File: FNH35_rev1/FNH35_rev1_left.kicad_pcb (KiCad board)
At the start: 2 copper layers, 127.2 x 116.7 mm, 117 parts, among them IC1 NUF2221W1T2G, J101 Conn_01x03, J102 DX07B024JJ3R1600, J103 Conn_01x08, K201 KEYSW, K202 KEYSW, K203 KEYSW, K204 KEYSW, K205 KEYSW, K206 KEYSW, K207 KEYSW, K208 KEYSW, K209 KEYSW, K210 KEYSW, K211 KEYSW, K212 KEYSW, K213 KEYSW, K214 KEYSW, K215 KEYSW, K216 KEYSW, K217 KEYSW, K218 KEYSW, SW101 SW_PUSH, U101 LD1117S33TR_SOT223, U102 STM32F303CCTx, U103 74AHCT125, X101 XTAL_GND

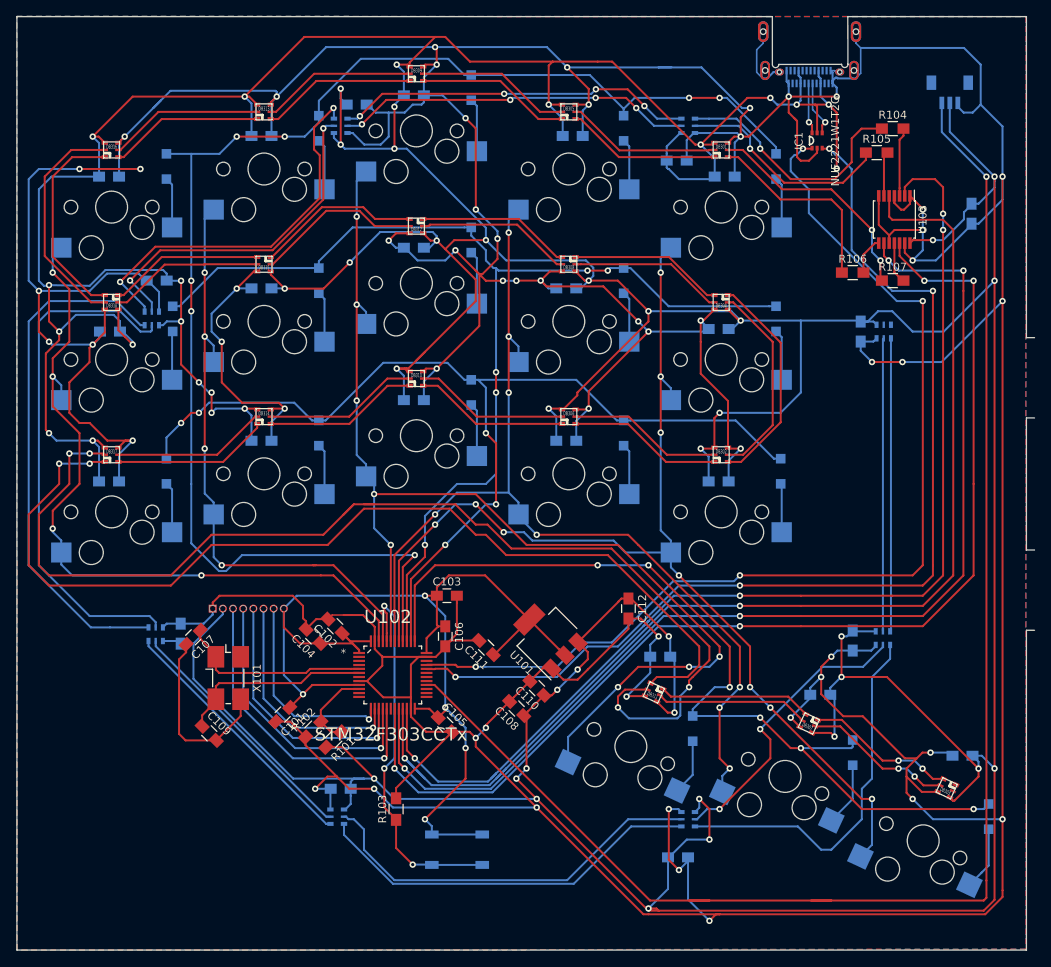
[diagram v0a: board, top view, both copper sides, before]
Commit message: left half crystal reworked
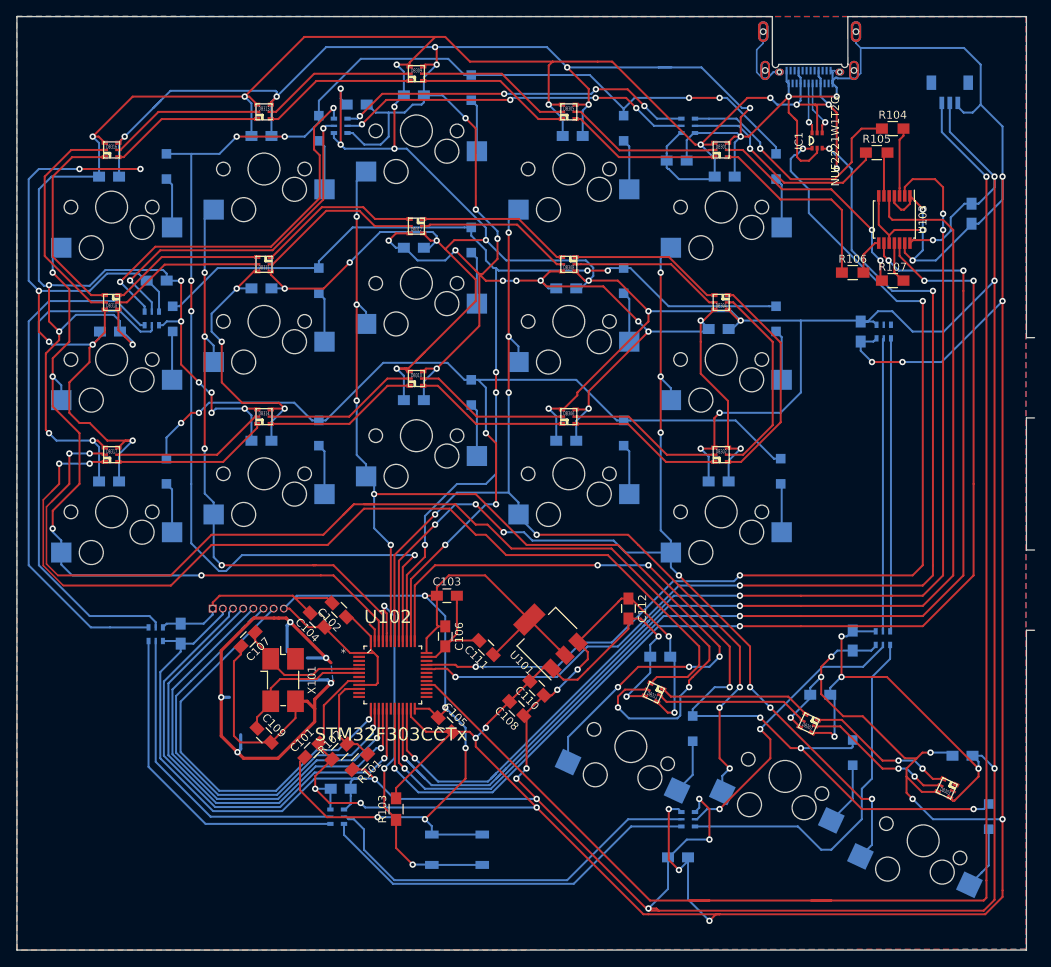
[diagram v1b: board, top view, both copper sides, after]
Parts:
- moved C107 6.86 mm to (44.0, 122.0)
- moved C109 6.86 mm to (46.0, 134.0)
- moved X101 6.86 mm to (48.4, 127.1)
- moved C101 5.76 mm to (52.0, 135.9), turned to 45 degrees
- moved R101 4.33 mm to (58.0, 137.4)
- moved R102 4.33 mm to (55.4, 136.1)
- moved C102 2.09 mm to (55.4, 118.4)
- moved C104 2.09 mm to (52.6, 119.6)
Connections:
- C107 pad 2: GND -> GNDA
- C109 pad 2: GND -> GNDA
- X101 pad 3: GND -> GNDA
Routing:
- net GNDA: track 0.00 -> 88.6 mm, vias 0 -> 5
- net GND: track 1063.1 -> 1011.8 mm
- net /LPA13: track 25.5 -> 53.4 mm
- net /LPA14: track 28.9 -> 55.7 mm
- net /LPA15: track 32.5 -> 57.2 mm
- net /LPA16: track 35.9 -> 59.1 mm
- net /LPA17: track 39.6 -> 61.0 mm
- net +5V: track 942.1 -> 951.2 mm
- net Net-(DR406-Pad2): track 32.6 -> 41.4 mm
- net Net-(DR406-Pad3): track 31.3 -> 39.8 mm
- net Net-(C107-Pad1): track 24.0 -> 16.5 mm
- net Net-(C109-Pad1): track 24.3 -> 17.9 mm
- net +3V3: track 144.6 -> 150.2 mm
- net Net-(DB311-Pad2): track 125.4 -> 122.8 mm
- net /LADC: track 10.4 -> 12.4 mm
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- added copper zone on B.Cu, net GNDA

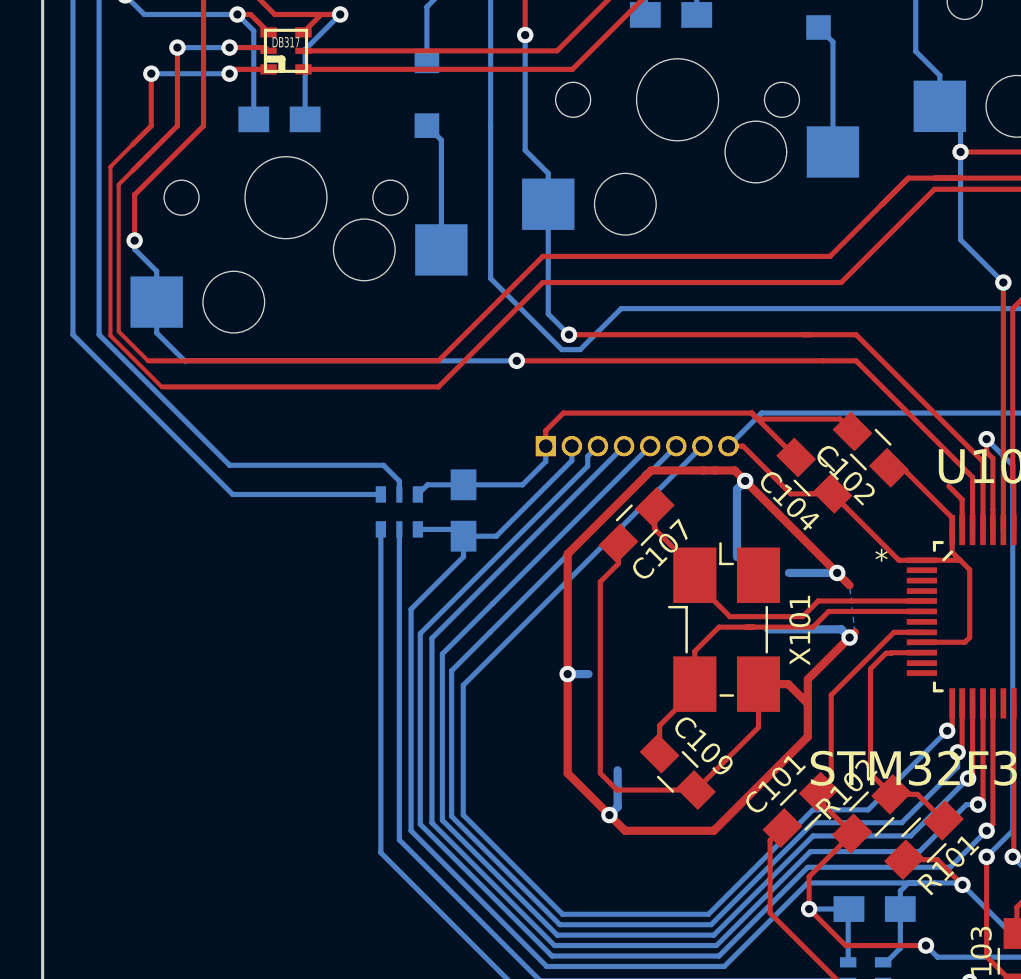
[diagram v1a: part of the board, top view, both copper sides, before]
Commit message: separated and rework crystal on right half
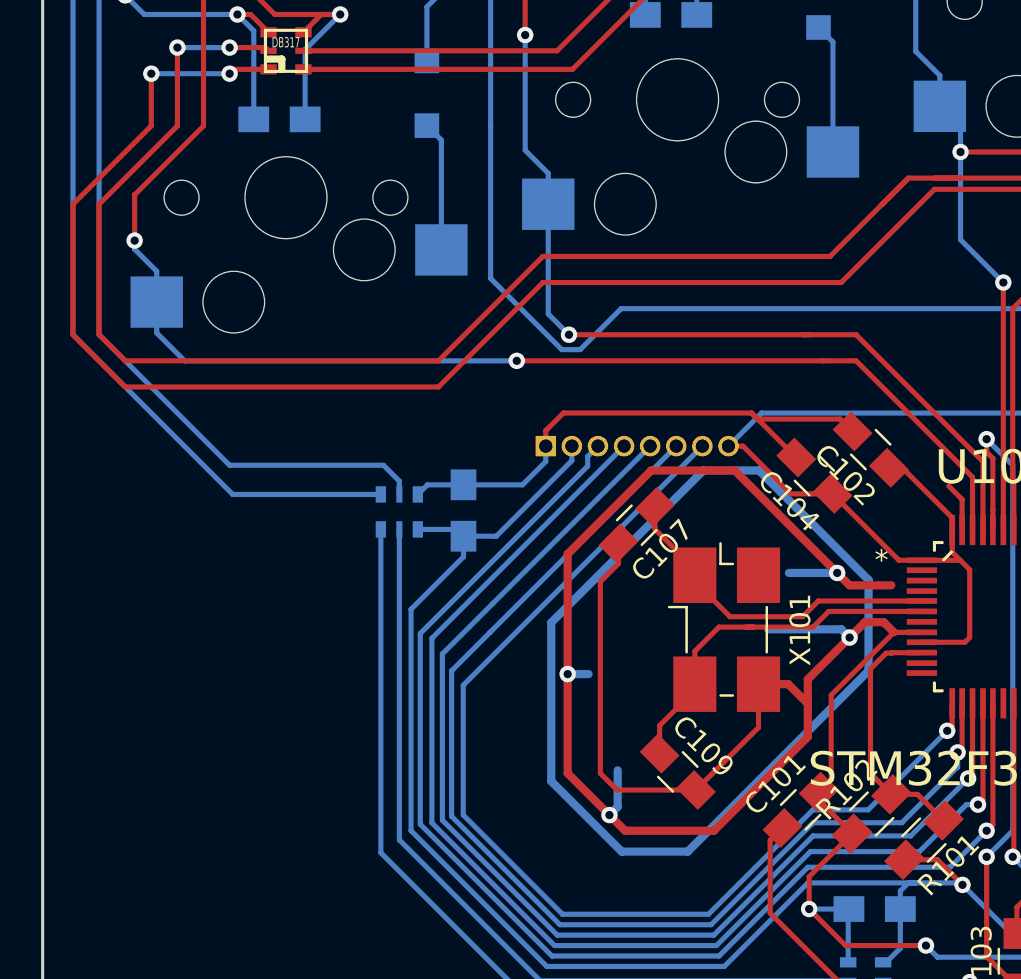
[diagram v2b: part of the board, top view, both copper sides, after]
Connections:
- C107 pad 2: GNDA -> GND
- C109 pad 2: GNDA -> GND
- X101 pad 3: GNDA -> GND
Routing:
- net GND: track 1011.8 -> 1101.2 mm, vias 56 -> 60
- net GNDA: track 88.6 -> 0.00 mm, vias 5 -> 0
- net (no net): track 0.00 -> 53.3 mm
- net Net-(DB311-Pad2): track 122.8 -> 125.4 mm
- net Net-(DB311-Pad3): track 141.0 -> 142.5 mm
- removed copper zone on B.Cu, net GNDA

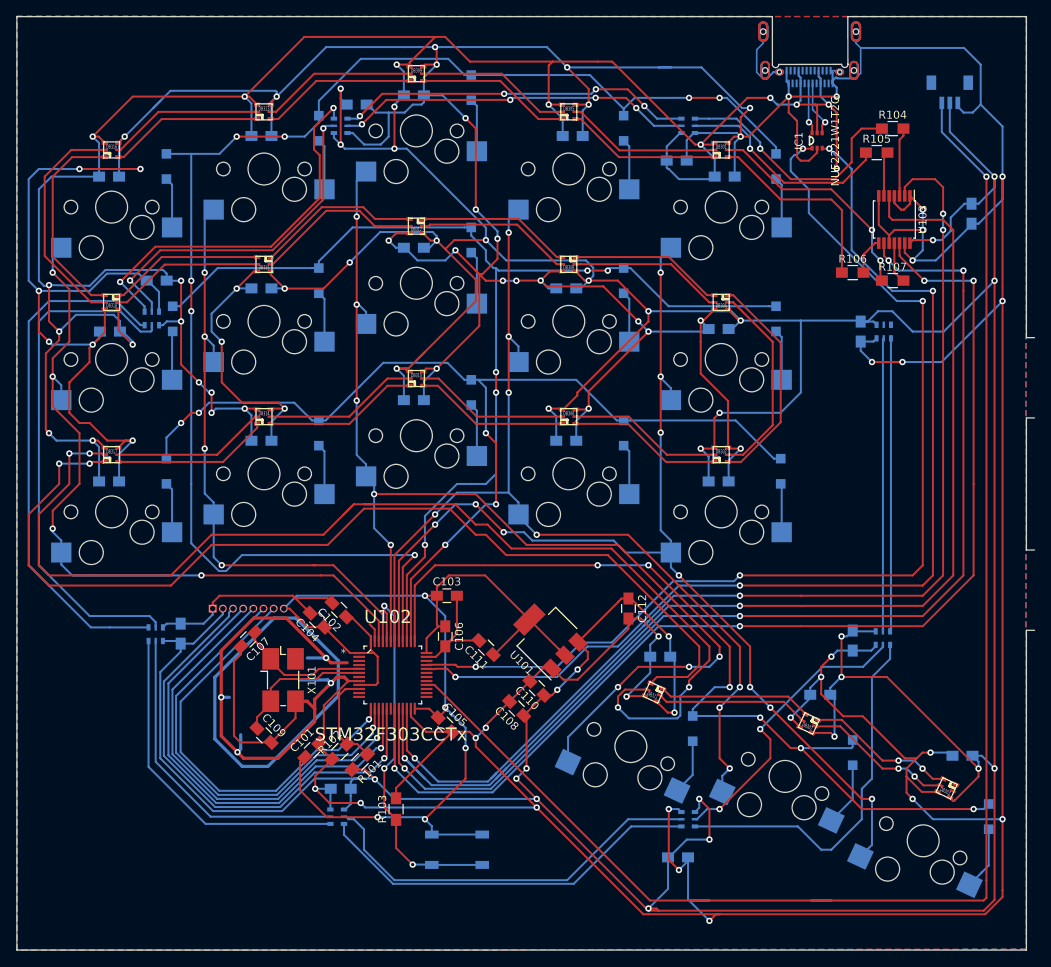
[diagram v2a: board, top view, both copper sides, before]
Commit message: GND and GNDD disconnected
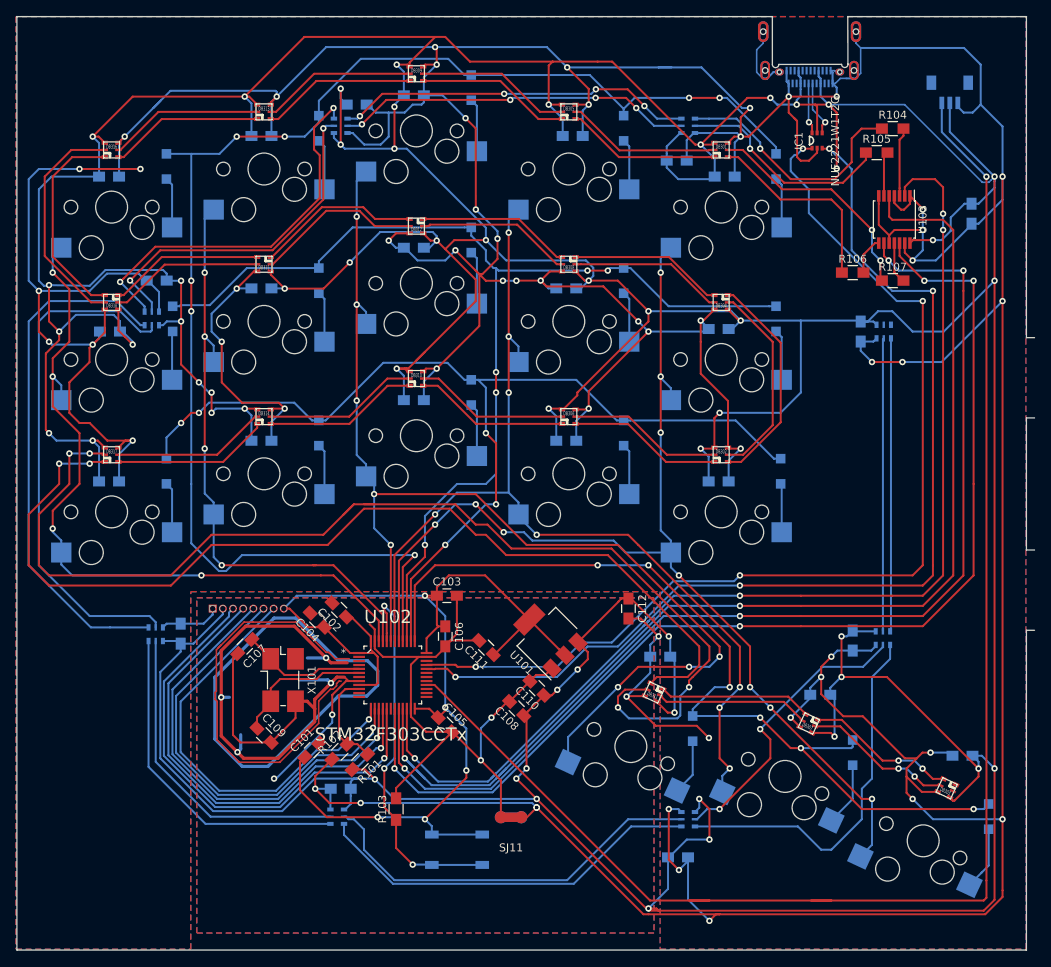
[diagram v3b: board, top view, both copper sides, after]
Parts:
- added SJ11: SOLDER_JUMPER, butts:gndcm, F.Cu at (76.9, 144.3)
- moved C107 0.98 mm to (43.6, 122.9)
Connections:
- C101 pad 2: GND -> GNDD
- C102 pad 2: GND -> GNDD
- C103 pad 2: GND -> GNDD
- C104 pad 2: GND -> GNDD
- C105 pad 2: GND -> GNDD
- C106 pad 2: GND -> GNDD
- C107 pad 2: GND -> GNDD
- C108 pad 2: GND -> GNDD
- C109 pad 2: GND -> GNDD
- C110 pad 2: GND -> GNDD
- C111 pad 2: GND -> GNDD
- R103 pad 2: GND -> GNDD
- U101 pad 1: GND -> GNDD
- U102 pad 23: GND -> GNDD
- U102 pad 35: GND -> GNDD
- U102 pad 47: GND -> GNDD
- U102 pad 8: GND -> GNDD
- X101 pad 3: GND -> GNDD
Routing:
- net GNDD: track 0.00 -> 185.6 mm, vias 0 -> 8
- net GND: track 1101.2 -> 916.1 mm, vias 60 -> 56
- net (no net): track 53.3 -> 116.2 mm
- net +5V: track 951.2 -> 976.2 mm
- net Net-(C107-Pad1): track 16.5 -> 15.8 mm
- added copper zone on B.Cu, net GNDD
- added copper zone on F.Cu, net GNDD
